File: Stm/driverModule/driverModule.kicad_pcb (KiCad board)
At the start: 4 copper layers, 88.4 x 67 mm, 41 parts, among them J1 Conn_02x05_Odd_Even, J101 Conn_02x13_Odd_Even, J102 DF40HC3.5-30DS-0.4V51, Q1 BSS138, Q2 BSS138, Q3 AON7410, U1 TLE94103EP, U102 ADM7171ACPZ-3.0-R7, U104 TPS5410DR, U201 DRV8838, U204 VNH5019A-E

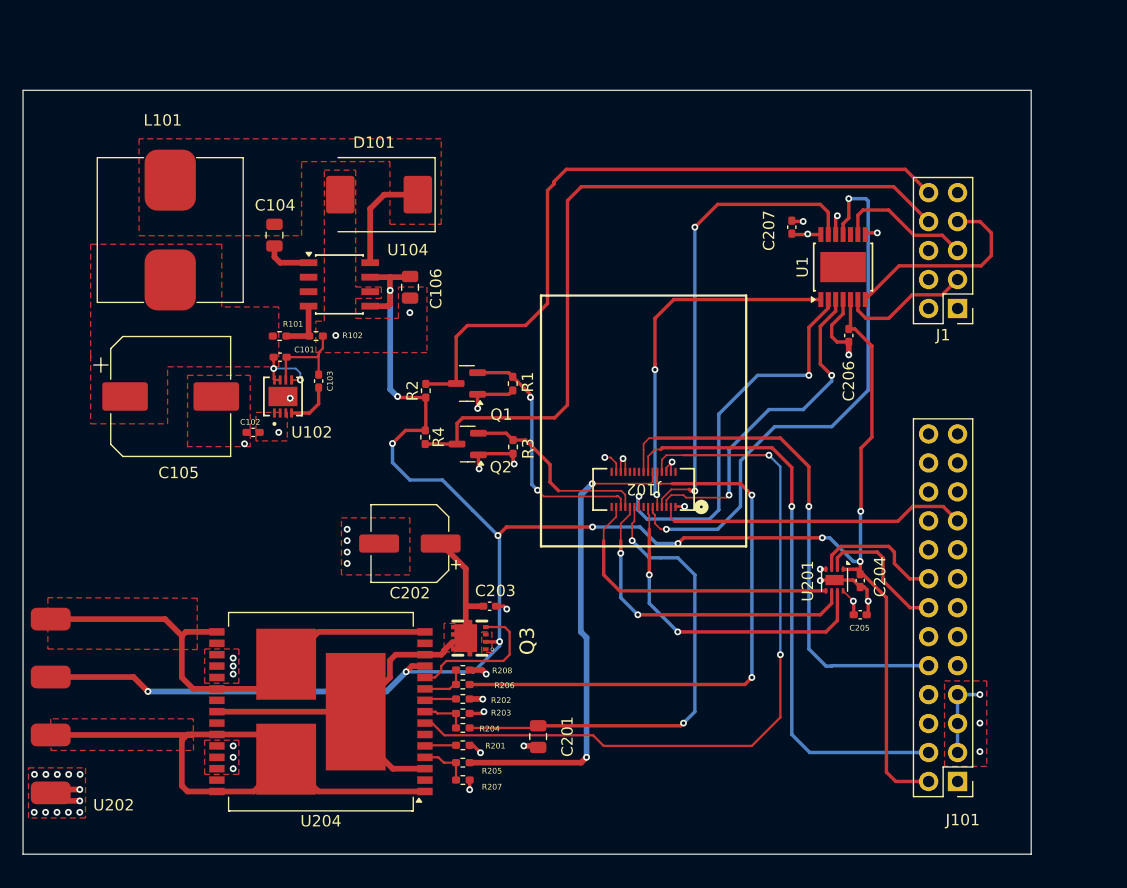
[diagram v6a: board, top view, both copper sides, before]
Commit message: Connectors
Remove some enable signals
Added Harness connectors
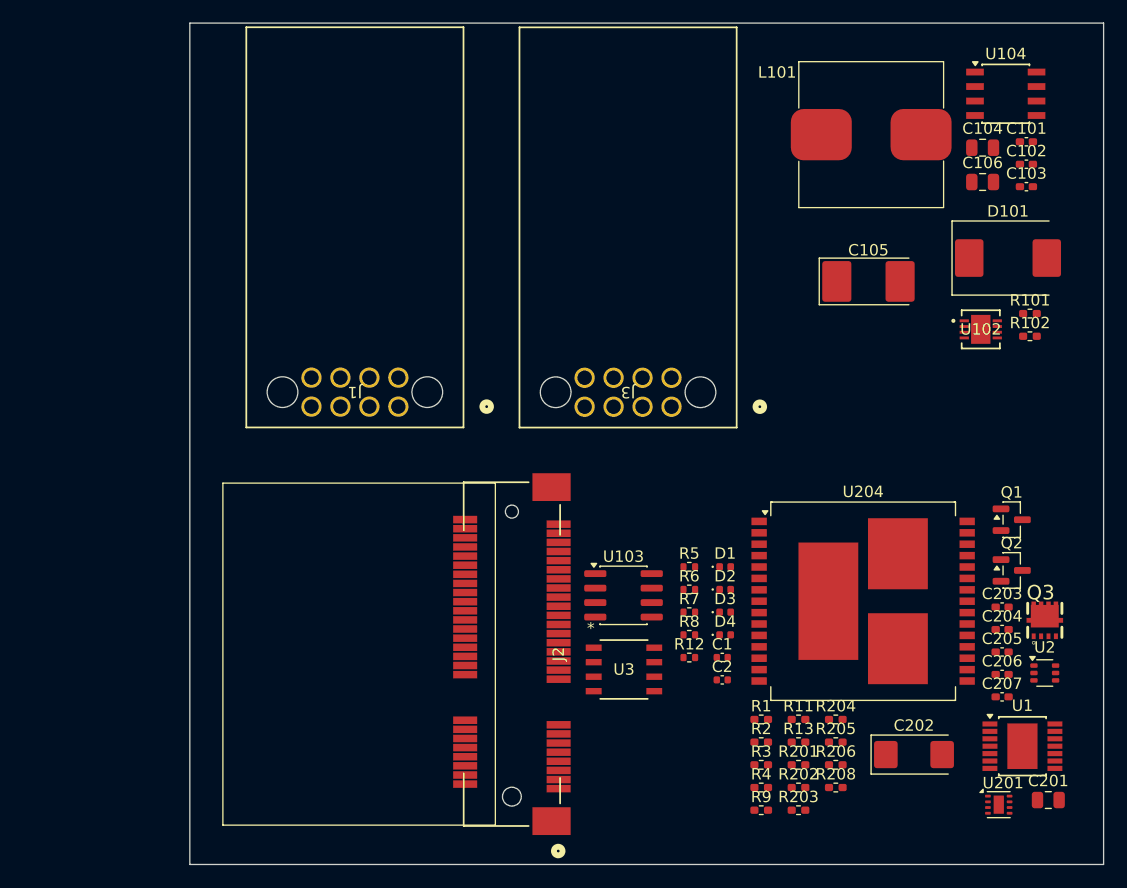
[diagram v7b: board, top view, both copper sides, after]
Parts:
- removed J101: Conn_02x13_Odd_Even, Connector_PinHeader_2.54mm:PinHeader_2x13_P2.54mm_Vertical
- removed J102: DF40HC3.5-30DS-0.4V51, con-hirose-df40:CONN_DF40HC3.5-30DS-0.4V51_HIR
- removed R207: 3K3, Resistor_SMD:R_0402_1005Metric_Pad0.72x0.64mm_HandSolder
- removed U202: ~, Local_Footprints:HeaderMotorCustomeSMD
- added C1: 1uF, Capacitor_SMD:C_0402_1005Metric, F.Cu at (160.9, 108.7)
- added C2: 100nF, Capacitor_SMD:C_0402_1005Metric, F.Cu at (160.9, 110.7)
- added D1: D, Diode_SMD:D_0402_1005Metric, F.Cu at (161.2, 100.8)
- added D2: D_Schottky, Diode_SMD:D_0402_1005Metric, F.Cu at (161.2, 102.8)
- added D3: D, Diode_SMD:D_0402_1005Metric, F.Cu at (161.2, 104.8)
- added D4: D_Schottky, Diode_SMD:D_0402_1005Metric, F.Cu at (161.2, 106.8)
- added J2: 2041119-1 (Mini Pcie Express Half), User_Footprint:CONN_2041119-1_TEC, F.Cu at (142.4, 108.5)
- added J3: 346916080, User_Footprint:CONN_SD-34691-601_08_MOL, F.Cu at (156.4, 86.8)
- added R11: 10K, Resistor_SMD:R_0402_1005Metric_Pad0.72x0.64mm_HandSolder, F.Cu at (167.6, 114.2)
- added R12: 10K, Resistor_SMD:R_0402_1005Metric, F.Cu at (158.0, 108.8)
- added R13: 10K, Resistor_SMD:R_0402_1005Metric_Pad0.72x0.64mm_HandSolder, F.Cu at (167.6, 116.2)
- added R5: 1K, Resistor_SMD:R_0402_1005Metric, F.Cu at (158.0, 100.8)
- added R6: R_US, Resistor_SMD:R_0402_1005Metric, F.Cu at (158.0, 102.8)
- added R7: 220K, Resistor_SMD:R_0402_1005Metric, F.Cu at (158.0, 104.8)
- added R8: 120, Resistor_SMD:R_0402_1005Metric, F.Cu at (158.0, 106.8)
- added R9: 10K, Resistor_SMD:R_0402_1005Metric_Pad0.72x0.64mm_HandSolder, F.Cu at (164.3, 122.1)
- added U103: TJA1051T-3, Package_SO:SOIC-8_3.9x4.9mm_P1.27mm, F.Cu at (152.2, 103.3)
- added U2: 74LVC2G04, Package_TO_SOT_SMD:SOT-363_SC-70-6, F.Cu at (189.2, 110.1)
- added U3: MCP2003B-E/SN, User_Footprint:SOIC8_SN_MCH, F.Cu at (152.3, 109.8)
- C105: footprint Capacitor_SMD:CP_Elec_10x10 -> Capacitor_Tantalum_SMD:CP_EIA-7132-20_AVX-U
- C202: footprint Capacitor_SMD:CP_Elec_6.3x5.4_Nichicon -> Capacitor_Tantalum_SMD:CP_EIA-6032-15_Kemet-U
- J1: value Conn_02x05_Odd_Even -> 346916080; footprint Connector_PinHeader_2.54mm:PinHeader_2x05_P2.54mm_Vertical -> User_Footprint:CONN_SD-34691-601_08_MOL
- L101: footprint Local_Footprints:L-SMD-13.45x12.6X5.0mm -> User_Footprint:L-SMD-13.45x12.6X5.0mm
- Q3: footprint Local_Footprints:DFN_3X3_EP -> User_Footprint:DFN_3X3_EP
- U102: footprint Local_Footprints:LFCSP-8-1EP_3x3mm_P0.5mm_EP_1.70x2.54mm -> User_Footprint:LFCSP-8-1EP_3x3mm_P0.5mm_EP_1.70x2.54mm
- U104: footprint Local_Footprints:SOIC-8-1EP_3.9x4.9mm_P1.27mm -> User_Footprint:SOIC-8-1EP_3.9x4.9mm_P1.27mm
- moved C102 71.8 mm to (187.6, 65.5), turned to 0 degrees
- moved C101 68.1 mm to (187.6, 63.5)
- moved R101 65.8 mm to (187.9, 78.6)
- moved C103 64.4 mm to (187.6, 67.5), turned to 0 degrees
- moved R102 62.6 mm to (187.9, 80.6)
- moved C104 62.6 mm to (183.7, 64.0), turned to 0 degrees
- moved L101 62.1 mm to (174.0, 62.9), turned to 0 degrees
- moved C105 62.0 mm to (173.7, 75.8)
- moved U102 61.5 mm to (183.6, 80.0), turned to 0 degrees
- moved U104 60.8 mm to (185.8, 59.3)
- moved D101 55.4 mm to (186.0, 73.7), turned to 0 degrees
- moved C106 51.1 mm to (183.7, 67.0), turned to 0 degrees
- moved Q3 50.5 mm to (189.2, 105.5), turned to 0 degrees
- moved J1 49.8 mm to (132.5, 86.7)
- moved Q1 49.3 mm to (186.3, 96.7), turned to 0 degrees
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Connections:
- net /BOOT renamed /Power/BOOT
- net /Motors/CS renamed /Motors Interface/CS
- net /Motors/G renamed /Motors Interface/G
- net /Motors/INA renamed /Motors Interface/INA
- net /Motors/Vout renamed /Motors Interface/Vout
- net /Motors/WindowMotorB renamed /Motors Interface/WindowMotorB
- net /Motors/WindwoMotorA renamed /Motors Interface/WindowMotorA
- net /PH renamed /Power/PH
- net /SS renamed /Power/SS
- net /VSENSE renamed /Power/VSENSE
- net KeyfobClose3v3 renamed /KeyfobClose3v3
- net KeyfobOpen3v3 renamed /KeyfobOpen3v3
- net WindowMotorCurrentSense renamed /WindowMotorCurrentSense
- J1 pad 1: unconnected-(J1-Pin_1-Pad1) -> /Harness/+12V
- J1 pad 2: unconnected-(J1-Pin_2-Pad2) -> /Harness/WindowMotorA
- J1 pad 3: /Motors/MirrorMotorXYB -> /Harness/WindowMotorB
- J1 pad 4: unconnected-(J1-Pin_4-Pad4) -> /Harness/LatchMotorA
- J1 pad 5: /Motors/MirrorMotorXA -> /Harness/LatchMotorB
- J1 pad 6: unconnected-(J1-Pin_6-Pad6) -> /Harness/MirrorMotorYA
- J1 pad 7: /Motors/MirrorMotorYA -> /Harness/MirrorMotorXA
- J1 pad 8: /Motors/KeyFobClose12V -> /Harness/MirrorMotorXYB
- Q1 pad 3: /Motors/keyFobOpen12V -> /Motors Interface/keyFobOpen12V
- Q2 pad 3: /Motors/KeyFobClose12V -> /Motors Interface/KeyFobClose12V
- R2 pad 2: /Motors/keyFobOpen12V -> /Motors Interface/keyFobOpen12V
- R201 pad 1: +3V3 -> /WindowMotorEnable
- R201 pad 2: /Motors/EN/DIAGA -> Net-(U204-EN/DIAGB)
- R202 pad 1: +3V3 -> /WindowMotorEnable
- R202 pad 2: /Motors/EN/DIAGB -> Net-(U204-EN/DIAGA)
- R205 pad 1: WindowMotorDirA -> Net-(R205-Pad1)
- R206 pad 1: WindowMotorDirB -> /WindowMotorDir
- R206 pad 2: /Motors/INB -> /Motors Interface/INB
- R208 pad 2: /Motors/INB -> /WindowMotorEnable
- R4 pad 2: /Motors/KeyFobClose12V -> /Motors Interface/KeyFobClose12V
- U1 pad 1: SpiMasterOutput -> /SpiMasterOutput
- U1 pad 11: MirrorMotorsEnable -> /Motors Interface/Enable
- U1 pad 13: SpiMasterInput -> /SpiMasterInput
- U1 pad 2: MirrorSpiChipSelect -> /MirrorSpiChipSelect
- U1 pad 3: SpiClock -> /SpiClock
- U1 pad 6: /Motors/MirrorMotorXYB -> /Motors Interface/MirrorMotorXYB
- U1 pad 7: /Motors/MirrorMotorYA -> /Motors Interface/MirrorMotorYA
- U1 pad 9: /Motors/MirrorMotorXA -> /Motors Interface/MirrorMotorXA
- U201 pad 2: LatchMotorA -> /Motors Interface/LatchMotorA
- U201 pad 3: LatchMotorB -> /Motors Interface/LatchMotorB
- U201 pad 5: LatchMotorEnable -> /LatchMotorEnable
- U201 pad 6: LatchMotorDirection -> /LatchMotorDirection
- U201 pad 7: nSleep -> Net-(U201-~{SLEEP})
- U204 pad 10: /Motors/INB -> /Motors Interface/INB
- U204 pad 5: /Motors/EN/DIAGA -> Net-(U204-EN/DIAGA)
- U204 pad 7: WindowMotorPWM -> Net-(U204-PWM)
- U204 pad 9: /Motors/EN/DIAGB -> Net-(U204-EN/DIAGB)
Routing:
- net +12V: track 177.8 -> 0.00 mm, vias 12 -> 0
- net WindowMotorPWM: track 67.1 -> 0.00 mm, vias 2 -> 0
- net /Motors/KeyFobClose12V: track 66.4 -> 0.00 mm
- net /Motors/keyFobOpen12V: track 61.1 -> 0.00 mm
- net /LatchSensorGreenConnector: track 51.1 -> 0.00 mm, vias 1 -> 0
- net WindowMotorDirB: track 50.7 -> 0.00 mm, vias 2 -> 0
- net /Motors Interface/WindowMotorA: track 50.6 -> 0.00 mm
- net MirrorMotorsEnable: track 49.6 -> 0.00 mm, vias 2 -> 0
- net GND: track 47.1 -> 0.00 mm, vias 42 -> 0
- net /LatchSensorPurpleConnector: track 45.3 -> 0.00 mm, vias 1 -> 0
- net /Motors Interface/Vout: track 44.7 -> 0.00 mm
- net /Motors Interface/WindowMotorB: track 42.8 -> 0.00 mm
- net SpiMasterInput: track 42.4 -> 0.00 mm, vias 2 -> 0
- net /WindowMotorCurrentSense: track 41.9 -> 0.00 mm, vias 2 -> 0
- net WindowMotorDirA: track 41.3 -> 0.00 mm, vias 2 -> 0
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- removed copper zone on F.Cu, net +12V
- removed copper zone on F.Cu, net +3V3
- removed copper zone on In2.Cu, net +3V3
- removed copper zone on F.Cu, net +5V
- removed copper zone on F.Cu, net /Motors Interface/Vout
- removed copper zone on F.Cu, net /Motors Interface/WindowMotorA
- removed copper zone on F.Cu, net /Motors Interface/WindowMotorB
- removed copper zone on F.Cu, net /Power/PH
- removed copper zone on F.Cu, net GND
- removed copper zone on In1.Cu, net GND
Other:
- board size 88.4 x 67 mm -> 80.1 x 73.8 mm

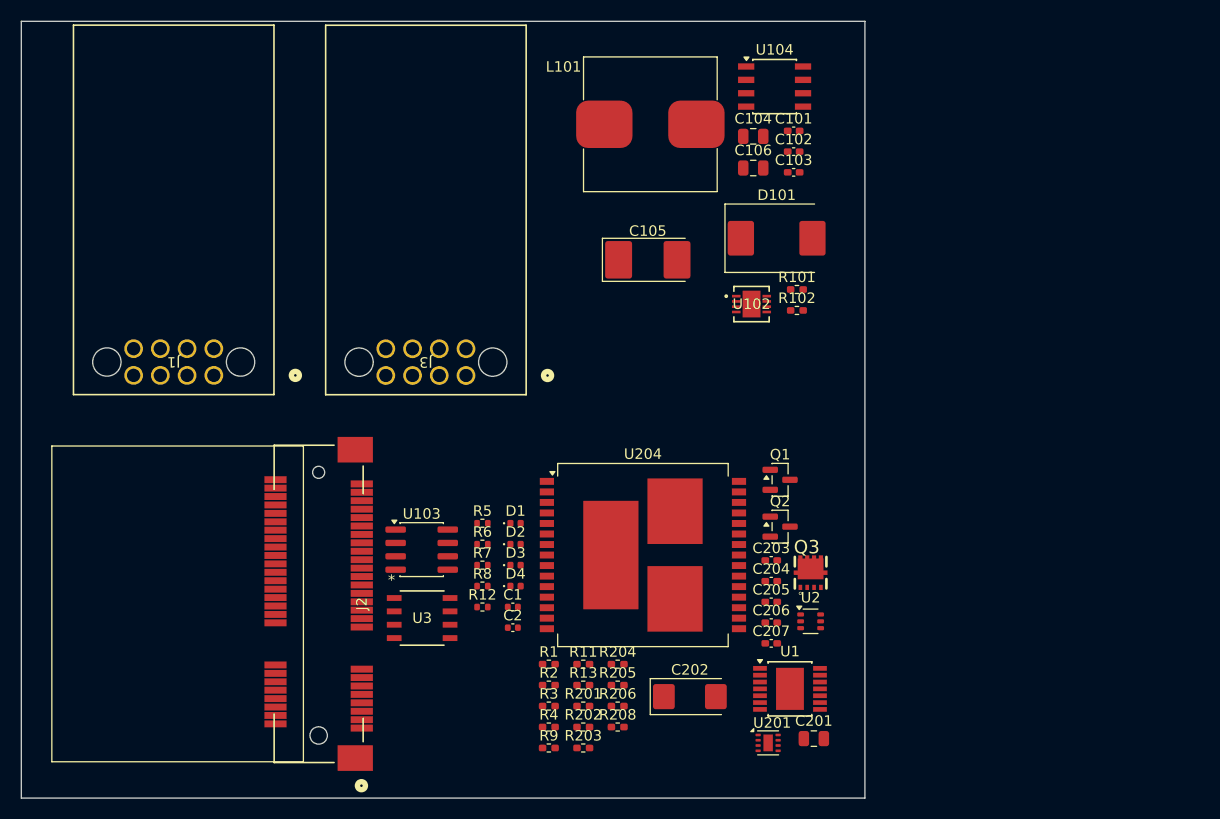
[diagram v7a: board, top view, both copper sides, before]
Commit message: libraries
Add new molex connectors
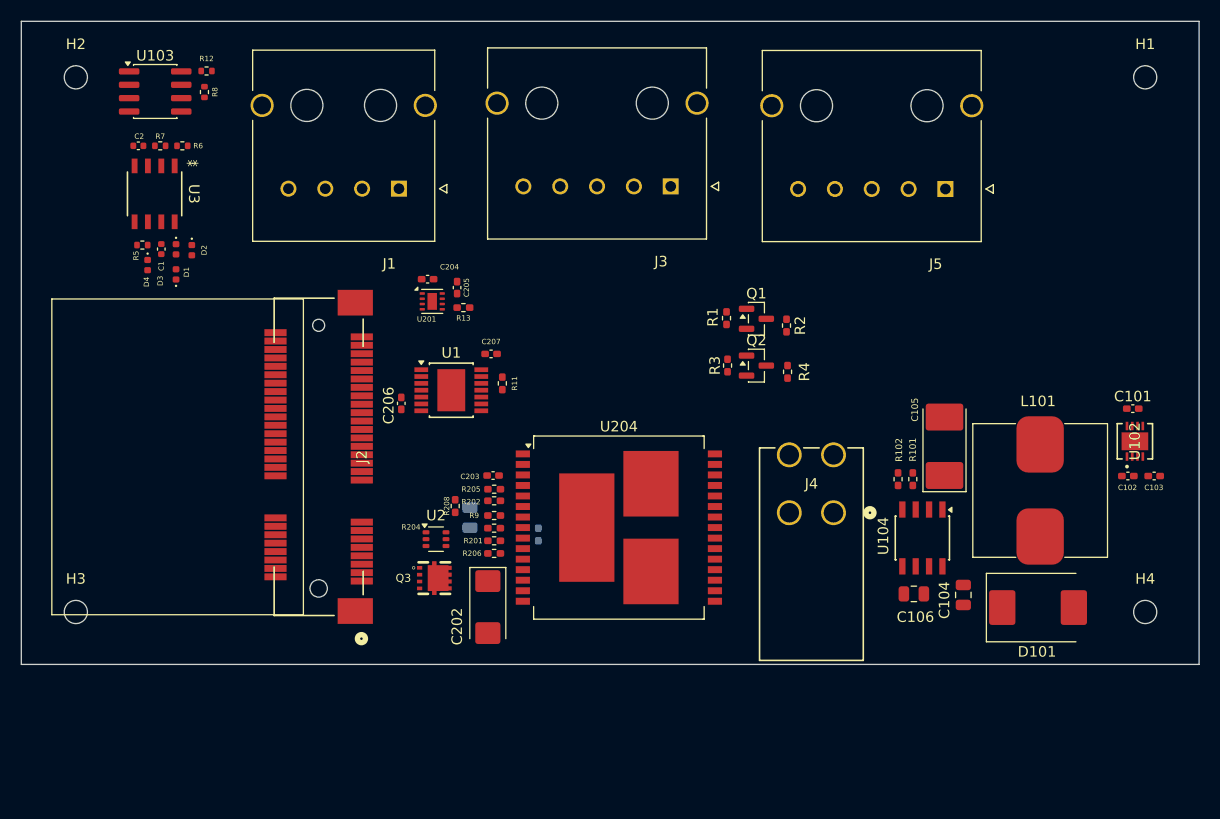
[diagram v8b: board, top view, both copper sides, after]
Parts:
- added H1: MountingHole, MountingHole:MountingHole_2.2mm_M2, F.Cu at (221.0, 58.4)
- added H2: MountingHole, MountingHole:MountingHole_2.2mm_M2, F.Cu at (119.4, 58.4)
- added H3: MountingHole, MountingHole:MountingHole_2.2mm_M2, F.Cu at (119.4, 109.2)
- added H4: MountingHole, MountingHole:MountingHole_2.2mm_M2, F.Cu at (221.0, 109.2)
- added J4: 353180420, User_Footprint:CONN_35318-0420_MOL, F.Cu at (191.4, 99.8)
- added J5: 1723103105, User_Footprint:MOLEX_1723103105, F.Cu at (202.0, 69.0)
- C201, R203: moved to B.Cu
- J1: value 346916080 -> 1723104104; footprint User_Footprint:CONN_SD-34691-601_08_MOL -> User_Footprint:MOLEX_1723104104
- J3: value 346916080 -> 1723103105; footprint User_Footprint:CONN_SD-34691-601_08_MOL -> User_Footprint:MOLEX_1723103105
- moved C2 58.0 mm to (125.3, 64.9), turned to 180 degrees
- moved R12 57.3 mm to (131.8, 57.8)
- moved R8 53.9 mm to (131.6, 59.8), turned to -90 degrees
- moved U201 52.7 mm to (153.2, 79.7)
- moved L101 50.8 mm to (211.0, 97.7), turned to -90 degrees
- moved U103 50.4 mm to (126.9, 59.8)
- moved R7 50.2 mm to (127.4, 64.9), turned to 180 degrees
- moved C104 47.9 mm to (203.7, 107.6), turned to -90 degrees
- moved C1 47.7 mm to (127.5, 74.7), turned to -90 degrees
- moved U3 47.7 mm to (126.9, 69.5), turned to -90 degrees
- moved R6 47.4 mm to (129.5, 64.9)
- moved D4 46.4 mm to (126.2, 76.3), turned to -90 degrees
- moved U104 45.1 mm to (199.8, 102.2), turned to -90 degrees
- moved C103 44.8 mm to (221.8, 96.3)
- moved C102 44.3 mm to (219.3, 96.3)
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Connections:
- J1 pad 1: /Harness/+12V -> GND
- J1 pad 2: /Harness/WindowMotorA -> /CAN_H
- J1 pad 3: /Harness/WindowMotorB -> /CAN_L
- J1 pad 4: /Harness/LatchMotorA -> /LIN_BUS
- J3 pad 1: /Harness/LatchSensorGreenConnector -> /Harness/MirrorMotorXYB
- J3 pad 2: /Harness/LatchSensorPurpleConnector -> /Harness/MirrorMotorXA
- J3 pad 3: /Harness/LatchPositionThroughSignal -> /Harness/MirrorMotorYA
- J3 pad 4: /Harness/KeyFobClose12V -> /Harness/LatchMotorB
- J3 pad 5: /Harness/keyFobOpen12V -> /Harness/LatchMotorA
- Q1 pad 3: /Motors Interface/keyFobOpen12V -> /Harness/keyFobOpen12V
- Q2 pad 3: /Motors Interface/KeyFobClose12V -> /Harness/KeyFobClose12V
- R2 pad 2: /Motors Interface/keyFobOpen12V -> /Harness/keyFobOpen12V
- R4 pad 2: /Motors Interface/KeyFobClose12V -> /Harness/KeyFobClose12V
- U1 pad 6: /Motors Interface/MirrorMotorXYB -> /Harness/MirrorMotorXYB
- U1 pad 7: /Motors Interface/MirrorMotorYA -> /Harness/MirrorMotorXA
- U1 pad 9: /Motors Interface/MirrorMotorXA -> /Harness/MirrorMotorYA
- U201 pad 2: /Motors Interface/LatchMotorA -> /Harness/LatchMotorA
- U201 pad 3: /Motors Interface/LatchMotorB -> /Harness/LatchMotorB
- U204 pad 1: /Motors Interface/WindowMotorA -> /Harness/WindowMotorA
- U204 pad 15: /Motors Interface/WindowMotorB -> /Harness/WindowMotorB
- U204 pad 16: /Motors Interface/WindowMotorB -> /Harness/WindowMotorB
- U204 pad 21: /Motors Interface/WindowMotorB -> /Harness/WindowMotorB
- U204 pad 25: /Motors Interface/WindowMotorA -> /Harness/WindowMotorA
- U204 pad 30: /Motors Interface/WindowMotorA -> /Harness/WindowMotorA
- U204 pad 32: /Motors Interface/WindowMotorB -> /Harness/WindowMotorB
- U204 pad 33: /Motors Interface/WindowMotorA -> /Harness/WindowMotorA
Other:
- board size 80.1 x 73.8 mm -> 111.9 x 61.1 mm
